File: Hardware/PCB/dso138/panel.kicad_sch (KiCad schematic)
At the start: 5 parts, among them J18 Conn_Coaxial_BNC, J19 AudioJack2, J20 AudioJack2, SW10 SW_SPDT, SW9 SW_SPST

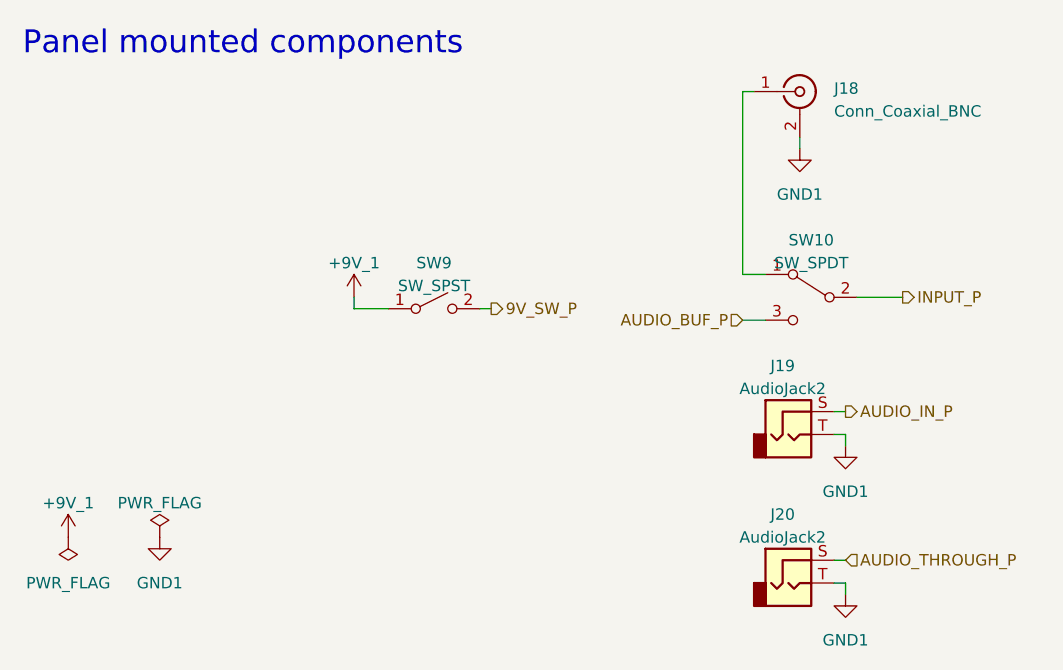
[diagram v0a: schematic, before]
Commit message: Net classes, move 7809 and make horizontal, inverting buffers, power switch via PCB
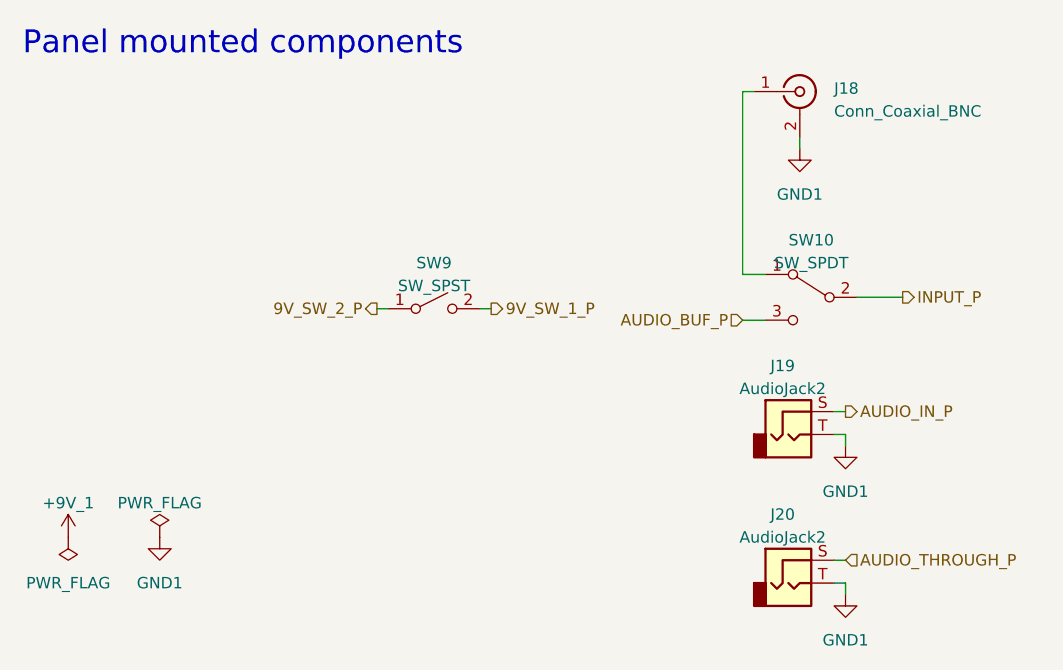
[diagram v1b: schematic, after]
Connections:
- net +9V_1: no longer SW9.1 (A)
- net 9V_SW_P renamed 9V_SW_1_P
- new net 9V_SW_2_P: SW9.1 (A)
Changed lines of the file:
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@@
 (kicad_sch (version 20230121) (generator eeschema)
   (paper "A4")
-  (wire (pts (xy 92.71 76.2) (xy 96.52 76.2))
-    (stroke (width 0) (type default))
-  )
   (wire (pts (xy 106.68 76.2) (xy 107.95 76.2))
     (stroke (width 0) (type default))
@@
     (stroke (width 0) (type default))
   )
-  (wire (pts (xy 92.71 74.93) (xy 92.71 76.2))
-    (stroke (width 0) (type default))
-  )
   (wire (pts (xy 135.89 77.47) (xy 138.43 77.47))
     (stroke (width 0) (type default))
   )
   (wire (pts (xy 146.05 104.14) (xy 147.32 104.14))
+    (stroke (width 0) (type default))
+  )
+  (wire (pts (xy 95.25 76.2) (xy 96.52 76.2))
     (stroke (width 0) (type default))
   )
@@
     (effects (font (size 1.27 1.27)) (justify left))
   )
-  (hierarchical_label "9V_SW_P" (shape output) (at 107.95 76.2 0) (fields_autoplaced)
+  (hierarchical_label "9V_SW_1_P" (shape output) (at 107.95 76.2 0) (fields_autoplaced)
     (effects (font (size 1.27 1.27)) (justify left))
   )
   (hierarchical_label "AUDIO_IN_P" (shape output) (at 147.32 87.63 0) (fields_autoplaced)
     (effects (font (size 1.27 1.27)) (justify left))
+  )
+  (hierarchical_label "9V_SW_2_P" (shape output) (at 95.25 76.2 180) (fields_autoplaced)
+    (effects (font (size 1.27 1.27)) (justify right))
   )
   (hierarchical_label "AUDIO_BUF_P" (shape input) (at 135.89 77.47 180) (fields_autoplaced)
@@
         )
       )
-    )
-  )
-  (symbol (lib_id "AO_symbols:+9V_1") (at 92.71 74.93 0) (unit 1)
-    (in_bom yes) (on_board yes) (dnp no) (fields_autoplaced)
-    (property "Reference" "#PWR030" (at 92.71 78.74 0)
-      (effects (font (size 1.27 1.27)) hide)
-    )
-    (property "Value" "+9V_1" (at 92.71 71.12 0)
-      (effects (font (size 1.27 1.27)))
-    )
-    (property "Footprint" "" (at 92.71 74.93 0)
-      (effects (font (size 1.27 1.27)) hide)
-    )
-    (property "Datasheet" "" (at 92.71 74.93 0)
-      (effects (font (size 1.27 1.27)) hide)
-    )
-    (pin "1")
-    (instances
-      (project "dso138"
-        (path "/1fce46f5-2003-4c7e-915f-b9b7dfc679d7/61a13e01-de11-4372-a9c0-3a1b05f9c11a"
-          (reference "#PWR030") (unit 1)
-        )
-      )

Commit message: Mechanicals
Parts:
- renumbered J19 to J21, J20 to J22, J18 to J23
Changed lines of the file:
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@@
   (symbol (lib_id "Connector:Conn_Coaxial") (at 142.24 52.07 0) (unit 1)
     (in_bom yes) (on_board no) (dnp no)
-    (property "Reference" "J18" (at 146.05 51.7282 0)
+    (property "Reference" "J23" (at 146.05 51.7282 0)
       (effects (font (size 1.27 1.27)) (justify left))
     )
@@
       (project "dso138"
         (path "/1fce46f5-2003-4c7e-915f-b9b7dfc679d7/61a13e01-de11-4372-a9c0-3a1b05f9c11a"
-          (reference "J18") (unit 1)
-        )
-      )
-    )
-  )
-  (symbol (lib_id "power:PWR_FLAG") (at 60.96 101.6 0) (mirror x) (unit 1)
-    (in_bom yes) (on_board yes) (dnp no) (fields_autoplaced)
-    (property "Reference" "#FLG03" (at 60.96 103.505 0)
-      (effects (font (size 1.27 1.27)) hide)
-    )
-    (property "Value" "PWR_FLAG" (at 60.96 106.68 0)
-      (effects (font (size 1.27 1.27)))
-    )
-    (property "Footprint" "" (at 60.96 101.6 0)
-      (effects (font (size 1.27 1.27)) hide)
-    )
-    (property "Datasheet" "~" (at 60.96 101.6 0)
+          (reference "J23") (unit 1)
+        )
+      )
+    )
+  )
+  (symbol (lib_id "power:GND1") (at 142.24 58.42 0) (mirror y) (unit 1)
+    (in_bom yes) (on_board yes) (dnp no) (fields_autoplaced)
+    (property "Reference" "#PWR029" (at 142.24 64.77 0)
+      (effects (font (size 1.27 1.27)) hide)
+    )
+    (property "Value" "GND1" (at 142.24 63.5 0)
+      (effects (font (size 1.27 1.27)))
+    )
+    (property "Footprint" "" (at 142.24 58.42 0)
+      (effects (font (size 1.27 1.27)) hide)
+    )
+    (property "Datasheet" "" (at 142.24 58.42 0)
+      (effects (font (size 1.27 1.27)) hide)
+    )
+    (pin "1")
+    (instances
+      (project "dso138"
+        (path "/1fce46f5-2003-4c7e-915f-b9b7dfc679d7/61a13e01-de11-4372-a9c0-3a1b05f9c11a"
+          (reference "#PWR029") (unit 1)
+        )
+      )
+    )
+  )
+  (symbol (lib_id "power:PWR_FLAG") (at 71.12 101.6 0) (unit 1)
+    (in_bom yes) (on_board yes) (dnp no) (fields_autoplaced)
+    (property "Reference" "#FLG03" (at 71.12 99.695 0)
+      (effects (font (size 1.27 1.27)) hide)
+    )
+    (property "Value" "PWR_FLAG" (at 71.12 97.79 0)
+      (effects (font (size 1.27 1.27)))
+    )
+    (property "Footprint" "" (at 71.12 101.6 0)
+      (effects (font (size 1.27 1.27)) hide)
+    )
+    (property "Datasheet" "~" (at 71.12 101.6 0)
       (effects (font (size 1.27 1.27)) hide)
     )
@@
     )
   )
-  (symbol (lib_id "power:GND1") (at 142.24 58.42 0) (mirror y) (unit 1)
-    (in_bom yes) (on_board yes) (dnp no) (fields_autoplaced)
-    (property "Reference" "#PWR031" (at 142.24 64.77 0)
-      (effects (font (size 1.27 1.27)) hide)
-    )
-    (property "Value" "GND1" (at 142.24 63.5 0)
-      (effects (font (size 1.27 1.27)))
-    )
-    (property "Footprint" "" (at 142.24 58.42 0)
-      (effects (font (size 1.27 1.27)) hide)
-    )
-    (property "Datasheet" "" (at 142.24 58.42 0)
-      (effects (font (size 1.27 1.27)) hide)
-    )
-    (pin "1")
-    (instances
-      (project "dso138"
-        (path "/1fce46f5-2003-4c7e-915f-b9b7dfc679d7/61a13e01-de11-4372-a9c0-3a1b05f9c11a"
-          (reference "#PWR031") (unit 1)
-        )
-      )
-    )
-  )
-  (symbol (lib_id "power:PWR_FLAG") (at 71.12 101.6 0) (unit 1)
-    (in_bom yes) (on_board yes) (dnp no) (fields_autoplaced)
-    (property "Reference" "#FLG04" (at 71.12 99.695 0)
-      (effects (font (size 1.27 1.27)) hide)
-    )
-    (property "Value" "PWR_FLAG" (at 71.12 97.79 0)
-      (effects (font (size 1.27 1.27)))
-    )
-    (property "Footprint" "" (at 71.12 101.6 0)
-      (effects (font (size 1.27 1.27)) hide)
-    )
-    (property "Datasheet" "~" (at 71.12 101.6 0)
-      (effects (font (size 1.27 1.27)) hide)
-    )
-    (pin "1")
-    (instances
-      (project "dso138"
-        (path "/1fce46f5-2003-4c7e-915f-b9b7dfc679d7/61a13e01-de11-4372-a9c0-3a1b05f9c11a"
-          (reference "#FLG04") (unit 1)
-        )
-      )
-    )
-  )
   (symbol (lib_id "AO_symbols:SW_SPST") (at 101.6 76.2 0) (unit 1)
     (in_bom yes) (on_board no) (dnp no) (fields_autoplaced)
@@
   (symbol (lib_id "AO_symbols:AudioJack2") (at 140.97 106.68 0) (unit 1)
     (in_bom yes) (on_board no) (dnp no) (fields_autoplaced)
-    (property "Reference" "J20" (at 140.335 99.06 0)
+    (property "Reference" "J22" (at 140.335 99.06 0)
       (effects (font (size 1.27 1.27)))
     )
@@
       (project "dso138"
         (path "/1fce46f5-2003-4c7e-915f-b9b7dfc679d7/61a13e01-de11-4372-a9c0-3a1b05f9c11a"
-          (reference "J20") (unit 1)
+          (reference "J22") (unit 1)
         )
       )
@@
   (symbol (lib_id "power:GND1") (at 71.12 101.6 0) (unit 1)
     (in_bom yes) (on_board yes) (dnp no) (fields_autoplaced)
-    (property "Reference" "#PWR029" (at 71.12 107.95 0)
+    (property "Reference" "#PWR028" (at 71.12 107.95 0)
       (effects (font (size 1.27 1.27)) hide)
     )
@@
       (project "dso138"
         (path "/1fce46f5-2003-4c7e-915f-b9b7dfc679d7/61a13e01-de11-4372-a9c0-3a1b05f9c11a"
-          (reference "#PWR029") (unit 1)
+          (reference "#PWR028") (unit 1)
         )
       )
@@
   (symbol (lib_id "power:GND1") (at 147.32 91.44 0) (unit 1)
     (in_bom yes) (on_board yes) (dnp no) (fields_autoplaced)
-    (property "Reference" "#PWR032" (at 147.32 97.79 0)
+    (property "Reference" "#PWR030" (at 147.32 97.79 0)
       (effects (font (size 1.27 1.27)) hide)
     )
@@
       (project "dso138"
         (path "/1fce46f5-2003-4c7e-915f-b9b7dfc679d7/61a13e01-de11-4372-a9c0-3a1b05f9c11a"
-          (reference "#PWR032") (unit 1)
-        )
-      )
-    )
-  )
-  (symbol (lib_id "AO_symbols:+9V_1") (at 60.96 101.6 0) (unit 1)
-    (in_bom yes) (on_board yes) (dnp no) (fields_autoplaced)
-    (property "Reference" "#PWR028" (at 60.96 105.41 0)
-      (effects (font (size 1.27 1.27)) hide)
-    )
-    (property "Value" "+9V_1" (at 60.96 97.79 0)
-      (effects (font (size 1.27 1.27)))
-    )
-    (property "Footprint" "" (at 60.96 101.6 0)
-      (effects (font (size 1.27 1.27)) hide)
-    )
-    (property "Datasheet" "" (at 60.96 101.6 0)
-      (effects (font (size 1.27 1.27)) hide)
-    )
-    (pin "1")
-    (instances
-      (project "dso138"
-        (path "/1fce46f5-2003-4c7e-915f-b9b7dfc679d7/61a13e01-de11-4372-a9c0-3a1b05f9c11a"
-          (reference "#PWR028") (unit 1)
+          (reference "#PWR030") (unit 1)
         )
       )
@@
   (symbol (lib_id "AO_symbols:AudioJack2") (at 140.97 90.17 0) (unit 1)
     (in_bom yes) (on_board no) (dnp no) (fields_autoplaced)
-    (property "Reference" "J19" (at 140.335 82.55 0)
+    (property "Reference" "J21" (at 140.335 82.55 0)
       (effects (font (size 1.27 1.27)))
     )
@@
       (project "dso138"
         (path "/1fce46f5-2003-4c7e-915f-b9b7dfc679d7/61a13e01-de11-4372-a9c0-3a1b05f9c11a"
-          (reference "J19") (unit 1)
+          (reference "J21") (unit 1)
         )
       )
@@
   (symbol (lib_id "power:GND1") (at 147.32 107.95 0) (unit 1)
     (in_bom yes) (on_board yes) (dnp no) (fields_autoplaced)
-    (property "Reference" "#PWR033" (at 147.32 114.3 0)
+    (property "Reference" "#PWR031" (at 147.32 114.3 0)
       (effects (font (size 1.27 1.27)) hide)
     )
@@
       (project "dso138"
         (path "/1fce46f5-2003-4c7e-915f-b9b7dfc679d7/61a13e01-de11-4372-a9c0-3a1b05f9c11a"
-          (reference "#PWR033") (unit 1)
-        )
-      )
+          (reference "#PWR031") (unit 1)
+        )
+      )

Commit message: STL file; BOM; documentation
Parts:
- J23: Manufacturer (none) -> Molex; Part (none) -> 0731315003; SKU (none) -> WM5379-ND; Vendor (none) -> Digi-Key
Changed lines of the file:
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@@
+      (effects (font (size 1.27 1.27)) hide)
+    )
+    (property "Description" "BNC jack, panel mount" (at 142.24 52.07 0)
+      (effects (font (size 1.27 1.27)) hide)
+    )
+    (property "SKU" "WM5379-ND" (at 142.24 52.07 0)
+      (effects (font (size 1.27 1.27)) hide)
+    )
+    (property "Vendor" "Digi-Key" (at 142.24 52.07 0)
+      (effects (font (size 1.27 1.27)) hide)
+    )
+    (property "Manufacturer" "Molex" (at 142.24 52.07 0)
+      (effects (font (size 1.27 1.27)) hide)
+    )
+    (property "Part" "0731315003" (at 142.24 52.07 0)
       (effects (font (size 1.27 1.27)) hide)
     )
@@
     )
     (property "SKU" "A-3186 (SPDT, use as SPST)" (at 101.6 76.2 0)
+      (effects (font (size 1.27 1.27)) hide)
+    )
+    (property "Description" "SPST toggle switch" (at 101.6 76.2 0)
       (effects (font (size 1.27 1.27)) hide)
     )
@@
       (effects (font (size 1.27 1.27)) hide)
     )
+    (property "Description" "SPDT toggle switch" (at 143.51 74.93 0)
+      (effects (font (size 1.27 1.27)) hide)
+    )
